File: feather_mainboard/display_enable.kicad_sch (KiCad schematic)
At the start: 5 parts, among them U2 2N7002K-T1-GE3, U3 SI2307CDS-T1-BE3

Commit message: schematic is almost done (check TODOs in schematic file)
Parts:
- renumbered R3 to R1, R1 to R3, U3 to U2, U2 to U3
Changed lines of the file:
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@@
 	(wire
 		(pts
-			(xy 137.16 87.63) (xy 137.16 90.17)
+			(xy 137.16 86.36) (xy 137.16 90.17)
 		)
 		(stroke
@@
 	(wire
 		(pts
-			(xy 123.19 123.19) (xy 123.19 124.46)
+			(xy 123.19 123.19) (xy 123.19 127)
 		)
 		(stroke
@@
 	(global_label "VCC"
 		(shape bidirectional)
-		(at 137.16 87.63 90)
+		(at 137.16 86.36 90)
 		(fields_autoplaced yes)
 		(effects
@@
 		)
 		(property "Intersheetrefs" "${INTERSHEET_REFS}"
-			(at 137.16 79.9049 90)
+			(at 137.16 78.6349 90)
 			(effects
 				(font
@@
 	(global_label "GND"
 		(shape bidirectional)
-		(at 123.19 124.46 270)
+		(at 123.19 127 270)
 		(fields_autoplaced yes)
 		(effects
@@
 		)
 		(property "Intersheetrefs" "${INTERSHEET_REFS}"
-			(at 123.19 132.427 90)
+			(at 123.19 134.967 90)
 			(effects
 				(font
@@
 		(on_board yes)
 		(dnp no)
-		(property "Reference" "U3"
+		(property "Reference" "U2"
 			(at 162.56 92.71 0)
 			(effects
@@
 			(project "feather_mainboard"
 				(path "/e1e12730-ab4f-45db-8b66-c1e0f78e2f00/e2a4e638-a577-4462-b00f-f16be15249be"
-					(reference "U3")
+					(reference "U2")
 					(unit 1)
 				)
@@
 		(on_board yes)
 		(dnp no)
-		(property "Reference" "R1"
+		(property "Reference" "R3"
 			(at 105.664 116.84 90)
 			(effects
@@
 			(project "feather_mainboard"
 				(path "/e1e12730-ab4f-45db-8b66-c1e0f78e2f00/e2a4e638-a577-4462-b00f-f16be15249be"
-					(reference "R1")
+					(reference "R3")
 					(unit 1)
 				)
@@
 		(on_board yes)
 		(dnp no)
-		(property "Reference" "U2"
+		(property "Reference" "U3"
 			(at 138.684 107.95 0)
 			(effects
@@
 			(project "feather_mainboard"
 				(path "/e1e12730-ab4f-45db-8b66-c1e0f78e2f00/e2a4e638-a577-4462-b00f-f16be15249be"
-					(reference "U2")
+					(reference "U3")
 					(unit 1)
 				)
@@
 		(on_board yes)
 		(dnp no)
-		(property "Reference" "R3"
+		(property "Reference" "R1"
 			(at 139.7 93.98 90)
 			(effects
@@
 			(project "feather_mainboard"
 				(path "/e1e12730-ab4f-45db-8b66-c1e0f78e2f00/e2a4e638-a577-4462-b00f-f16be15249be"
-					(reference "R3")
+					(reference "R1")
 					(unit 1)
 				)

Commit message: changed footprints location to match the new folder. TODO: check if the path is working on another computer
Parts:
- U2: footprint footprints:SOT-23_VIS -> Custom footprints:SOT-23_VIS
- U3: footprint footprints:SOT_02K-T1-GE3_VIS -> Custom footprints:SOT_02K-T1-GE3_VIS
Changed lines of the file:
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@@
 			)
 		)
-		(property "Footprint" "footprints:SOT-23_VIS"
+		(property "Footprint" "Custom footprints:SOT-23_VIS"
 			(at 142.24 99.06 0)
 			(effects
@@
 			)
 		)
-		(property "Footprint" "footprints:SOT_02K-T1-GE3_VIS"
+		(property "Footprint" "Custom footprints:SOT_02K-T1-GE3_VIS"
 			(at 124.46 110.49 0)
 			(effects

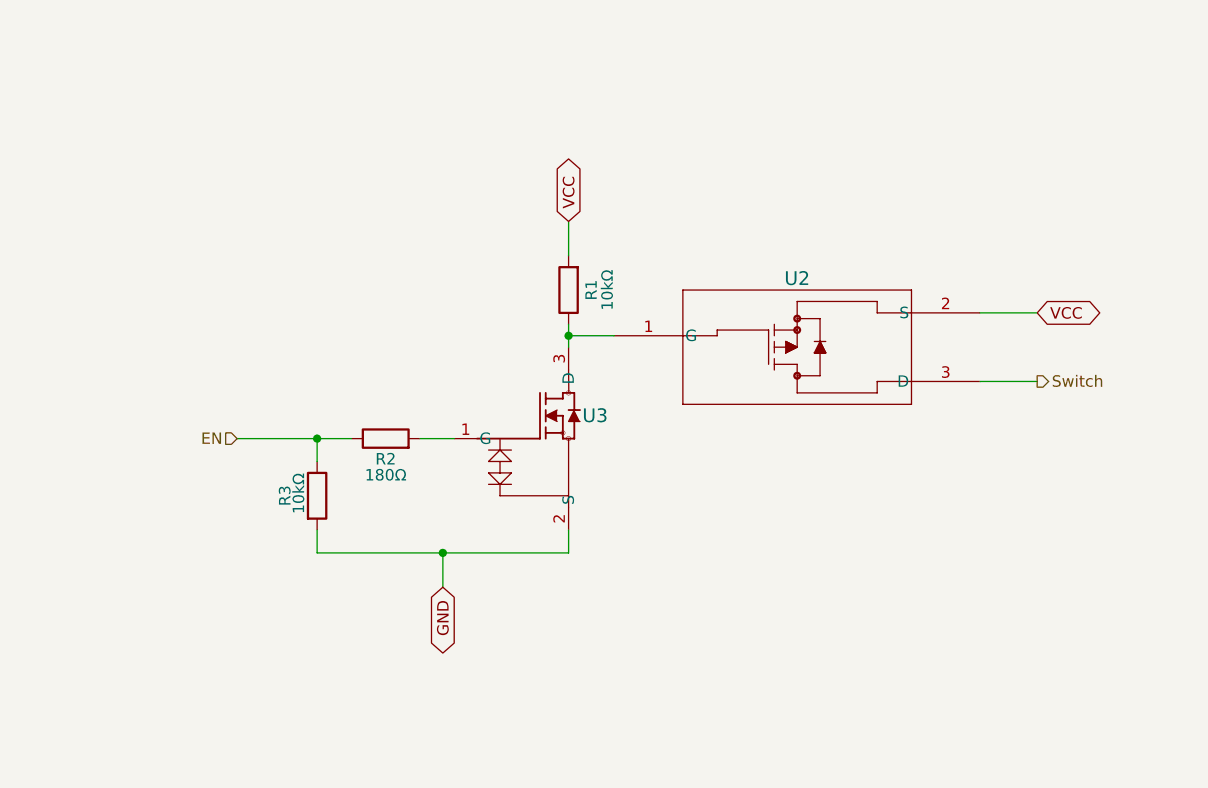
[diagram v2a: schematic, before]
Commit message: added daughter board
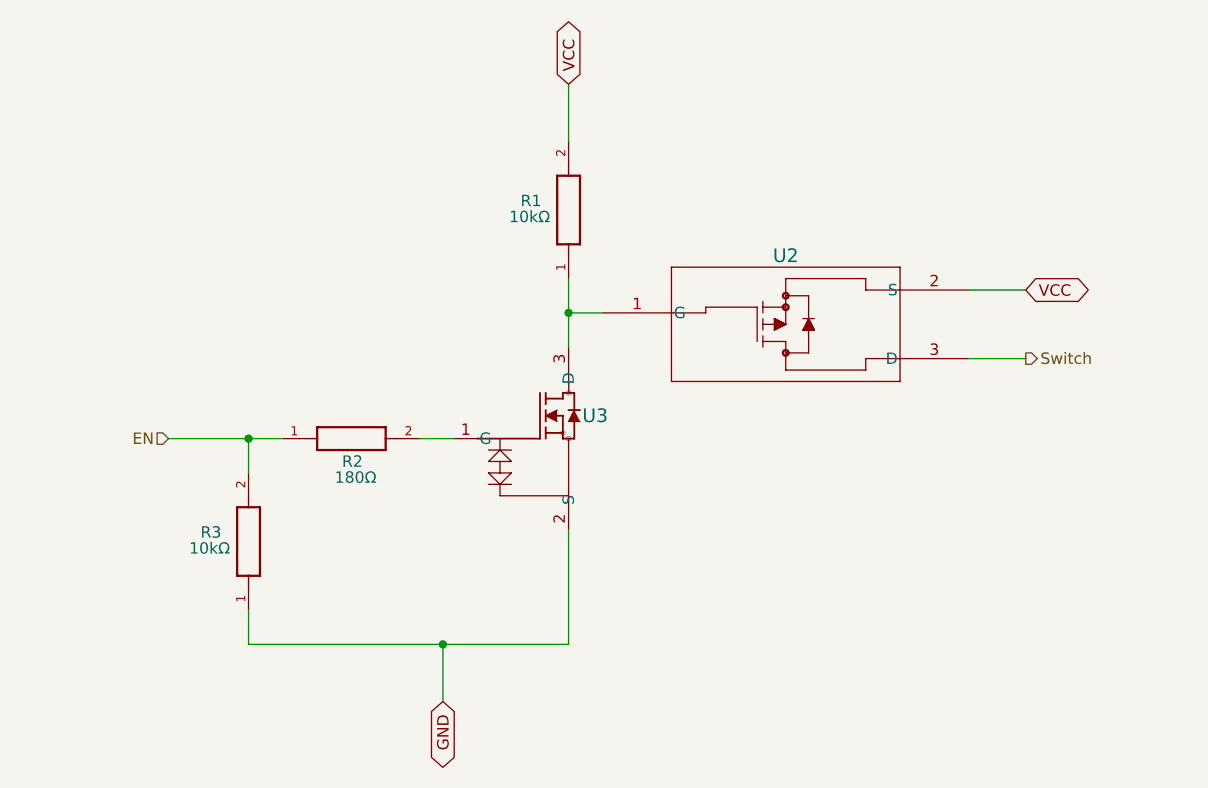
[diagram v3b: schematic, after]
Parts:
- removed R1, R3: 10kΩ, Resistor_SMD:R_0805_2012Metric_Pad1.20x1.40mm_HandSolder, symbol Device:R
- removed R2: 180Ω, Resistor_SMD:R_0805_2012Metric_Pad1.20x1.40mm_HandSolder, symbol Device:R
- added R1, R3: 10kΩ, Custom footprints:WRIS-RSKS_0603_REFLOW, symbol WRIS-RSKS_0603:WRIS-RSKS_0603
- added R2: 180Ω, Custom footprints:WRIS-RSKS_0603_REFLOW, symbol WRIS-RSKS_0603:WRIS-RSKS_0603
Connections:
- net EN: now also R2.1, R3.2
- net GND: now also R3.1
- net VCC: now also R1.2
- net at U3.1 (G): now also R2.2
- net at U2.1 (G), U3.3 (D): now also R1.1
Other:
- moved on the sheet: U2

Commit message: finished mainboard design, need to do the routing
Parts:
- renumbered R1 to R1_1, R3 to R1_2, R2 to R2_1
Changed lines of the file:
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@@
 	)
 	(hierarchical_label "Switch"
-		(shape output)
+		(shape bidirectional)
 		(at 187.96 101.6 0)
 		(fields_autoplaced yes)
@@
 	)
 	(hierarchical_label "EN"
-		(shape input)
+		(shape bidirectional)
 		(at 92.71 110.49 180)
 		(fields_autoplaced yes)
@@
 		(on_board yes)
 		(dnp no)
-		(property "Reference" "R2"
-			(at 114.3 113.03 0)
+		(property "Reference" "R2_1"
+			(at 115.57 113.03 0)
 			(effects
 				(font
@@
 			(project "feather_mainboard"
 				(path "/e1e12730-ab4f-45db-8b66-c1e0f78e2f00/e2a4e638-a577-4462-b00f-f16be15249be"
-					(reference "R2")
+					(reference "R2_1")
 					(unit 1)
 				)
@@
 		(on_board yes)
 		(dnp no)
-		(property "Reference" "R3"
-			(at 96.266 120.904 90)
+		(property "Reference" "R1_2"
+			(at 94.996 120.904 90)
 			(effects
 				(font
@@
 			(project "feather_mainboard"
 				(path "/e1e12730-ab4f-45db-8b66-c1e0f78e2f00/e2a4e638-a577-4462-b00f-f16be15249be"
-					(reference "R3")
+					(reference "R1_2")
 					(unit 1)
 				)
@@
 		(on_board yes)
 		(dnp no)
-		(property "Reference" "R1"
-			(at 131.826 84.074 90)
+		(property "Reference" "R1_1"
+			(at 130.556 84.074 90)
 			(effects
 				(font
@@
 			(project "feather_mainboard"
 				(path "/e1e12730-ab4f-45db-8b66-c1e0f78e2f00/e2a4e638-a577-4462-b00f-f16be15249be"
-					(reference "R1")
-					(unit 1)
-				)
+					(reference "R1_1")
+					(unit 1)
+				)

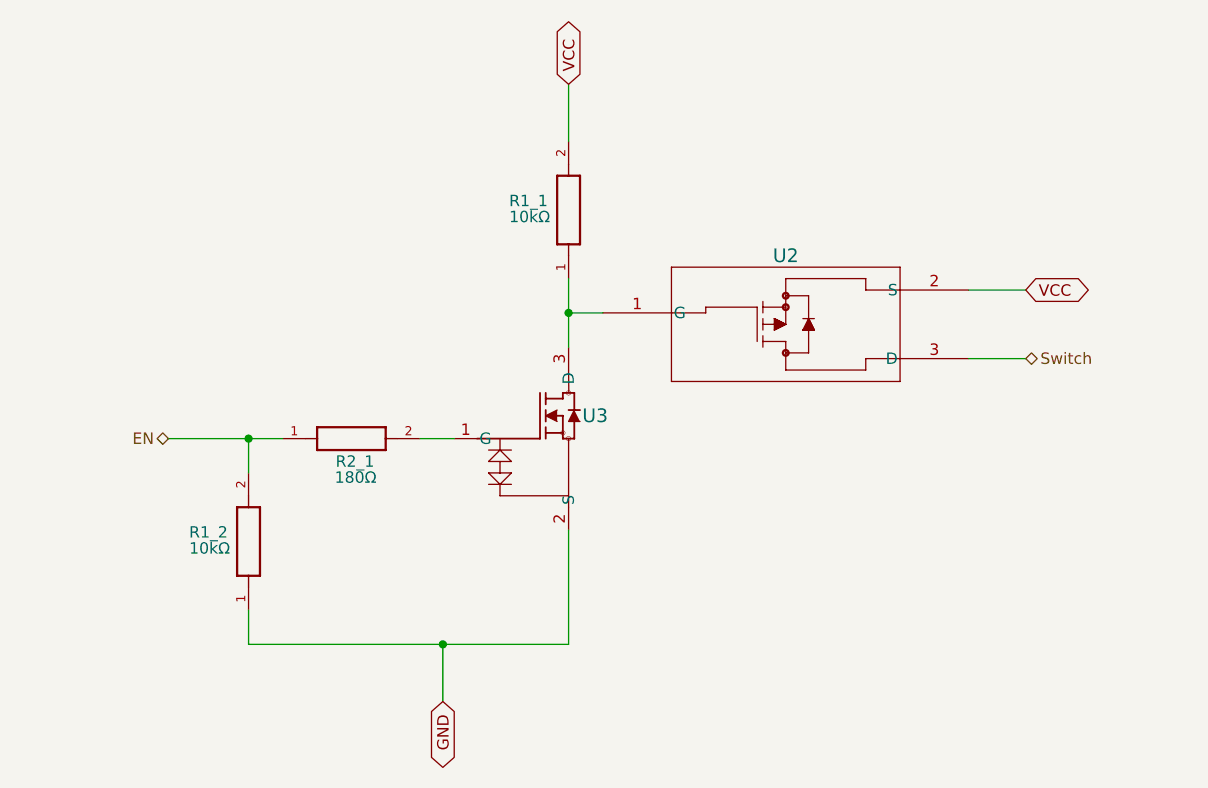
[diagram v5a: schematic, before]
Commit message: Updated the mainboard: removed unnecessary pull-ups on SD card lines; connected IIC pull-ups to enable circuit; cleaned up schematic
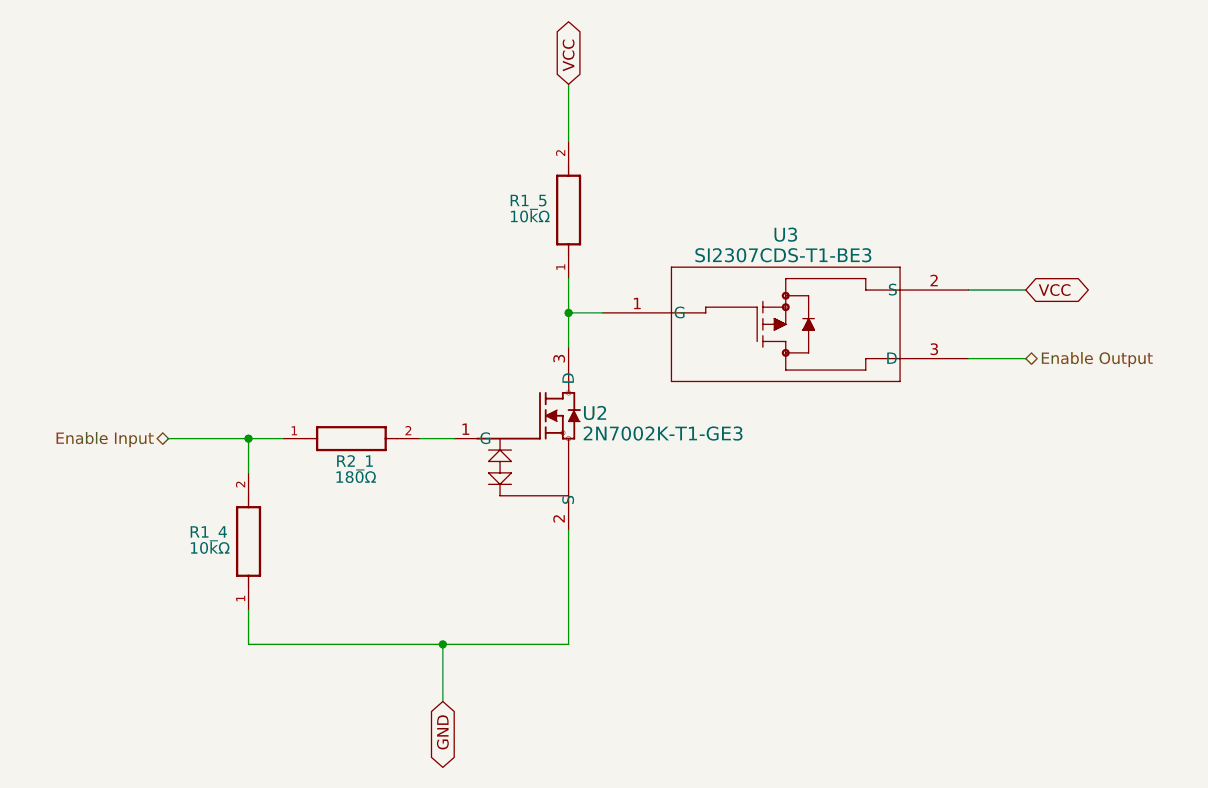
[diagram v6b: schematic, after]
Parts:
- renumbered R1_2 to R1_4, R1_1 to R1_5, U3 to U2, U2 to U3
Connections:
- net EN renamed Enable Input
- net Switch renamed Enable Output
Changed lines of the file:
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@@
 		)
 	)
-	(hierarchical_label "Switch"
+	(hierarchical_label "Enable Output"
 		(shape bidirectional)
 		(at 187.96 101.6 0)
+		(fields_autoplaced yes)
 		(effects
 			(font
@@
 		)
 	)
-	(hierarchical_label "EN"
+	(hierarchical_label "Enable Input"
 		(shape bidirectional)
 		(at 92.71 110.49 180)
+		(fields_autoplaced yes)
 		(effects
 			(font
@@
 		(instances
 			(project "feather_mainboard"
-				(path "/e1e12730-ab4f-45db-8b66-c1e0f78e2f00/e2a4e638-a577-4462-b00f-f16be15249be"
+				(path "/e1e12730-ab4f-45db-8b66-c1e0f78e2f00/45521865-6226-43e1-9fb7-931b1f23d3b1"
 					(reference "R2_1")
 					(unit 1)
@@
 		(on_board yes)
 		(dnp no)
-		(property "Reference" "U2"
-			(at 161.29 90.17 0)
+		(property "Reference" "U3"
+			(at 161.29 87.884 0)
 			(effects
 				(font
@@
 					(size 1.524 1.524)
 				)
-				(hide yes)
 			)
 		)
@@
 		(instances
 			(project "feather_mainboard"
-				(path "/e1e12730-ab4f-45db-8b66-c1e0f78e2f00/e2a4e638-a577-4462-b00f-f16be15249be"
-					(reference "U2")
+				(path "/e1e12730-ab4f-45db-8b66-c1e0f78e2f00/45521865-6226-43e1-9fb7-931b1f23d3b1"
+					(reference "U3")
 					(unit 1)
 				)
@@
 		(on_board yes)
 		(dnp no)
-		(property "Reference" "R1_2"
+		(property "Reference" "R1_4"
 			(at 94.996 120.904 90)
 			(effects
@@
 		(instances
 			(project "feather_mainboard"
-				(path "/e1e12730-ab4f-45db-8b66-c1e0f78e2f00/e2a4e638-a577-4462-b00f-f16be15249be"
-					(reference "R1_2")
+				(path "/e1e12730-ab4f-45db-8b66-c1e0f78e2f00/45521865-6226-43e1-9fb7-931b1f23d3b1"
+					(reference "R1_4")
 					(unit 1)
 				)
@@
 		(on_board yes)
 		(dnp no)
-		(property "Reference" "U3"
-			(at 138.684 107.95 0)
+		(property "Reference" "U2"
+			(at 138.684 107.696 0)
 			(effects
 				(font
@@
 				)
 				(justify left)
-				(hide yes)
 			)
 		)
@@
 		(instances
 			(project "feather_mainboard"
-				(path "/e1e12730-ab4f-45db-8b66-c1e0f78e2f00/e2a4e638-a577-4462-b00f-f16be15249be"
-					(reference "U3")
+				(path "/e1e12730-ab4f-45db-8b66-c1e0f78e2f00/45521865-6226-43e1-9fb7-931b1f23d3b1"
+					(reference "U2")
 					(unit 1)
 				)
@@
 		(on_board yes)
 		(dnp no)
-		(property "Reference" "R1_1"
+		(property "Reference" "R1_5"
 			(at 130.556 84.074 90)
 			(effects
@@
 		(instances
 			(project "feather_mainboard"
-				(path "/e1e12730-ab4f-45db-8b66-c1e0f78e2f00/e2a4e638-a577-4462-b00f-f16be15249be"
-					(reference "R1_1")
-					(unit 1)
-				)
+				(path "/e1e12730-ab4f-45db-8b66-c1e0f78e2f00/45521865-6226-43e1-9fb7-931b1f23d3b1"
+					(reference "R1_5")
+					(unit 1)
+				)
